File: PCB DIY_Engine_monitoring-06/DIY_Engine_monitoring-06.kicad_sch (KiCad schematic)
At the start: 62 parts, among them J1 test, J2 5V_P/S, J3 Barrel_Jack, U1 EL817, U2 EL817, U3 EL817, U4 EL817, U5 MEGA2560-Pro

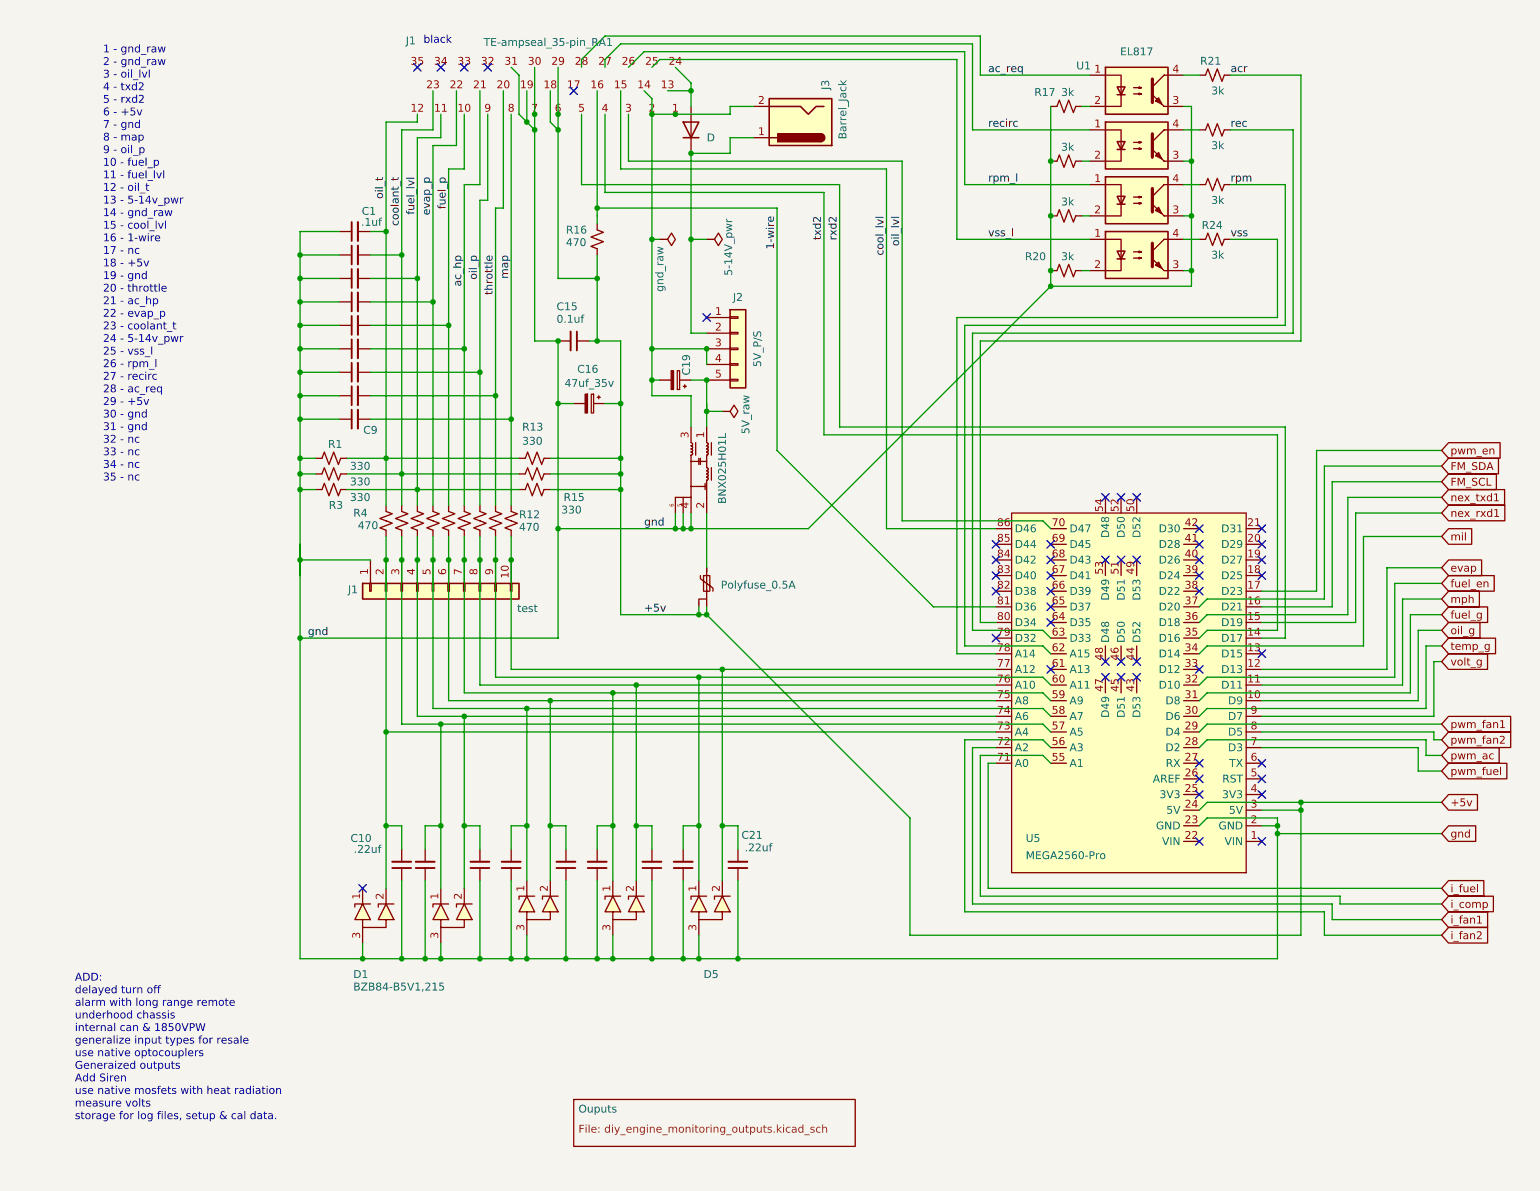
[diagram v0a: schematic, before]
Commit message: Updates include photos, harness drawings and code
Early prototype partally working.  Photos of Earlier version undergoing testing.  PCB files are for next version.
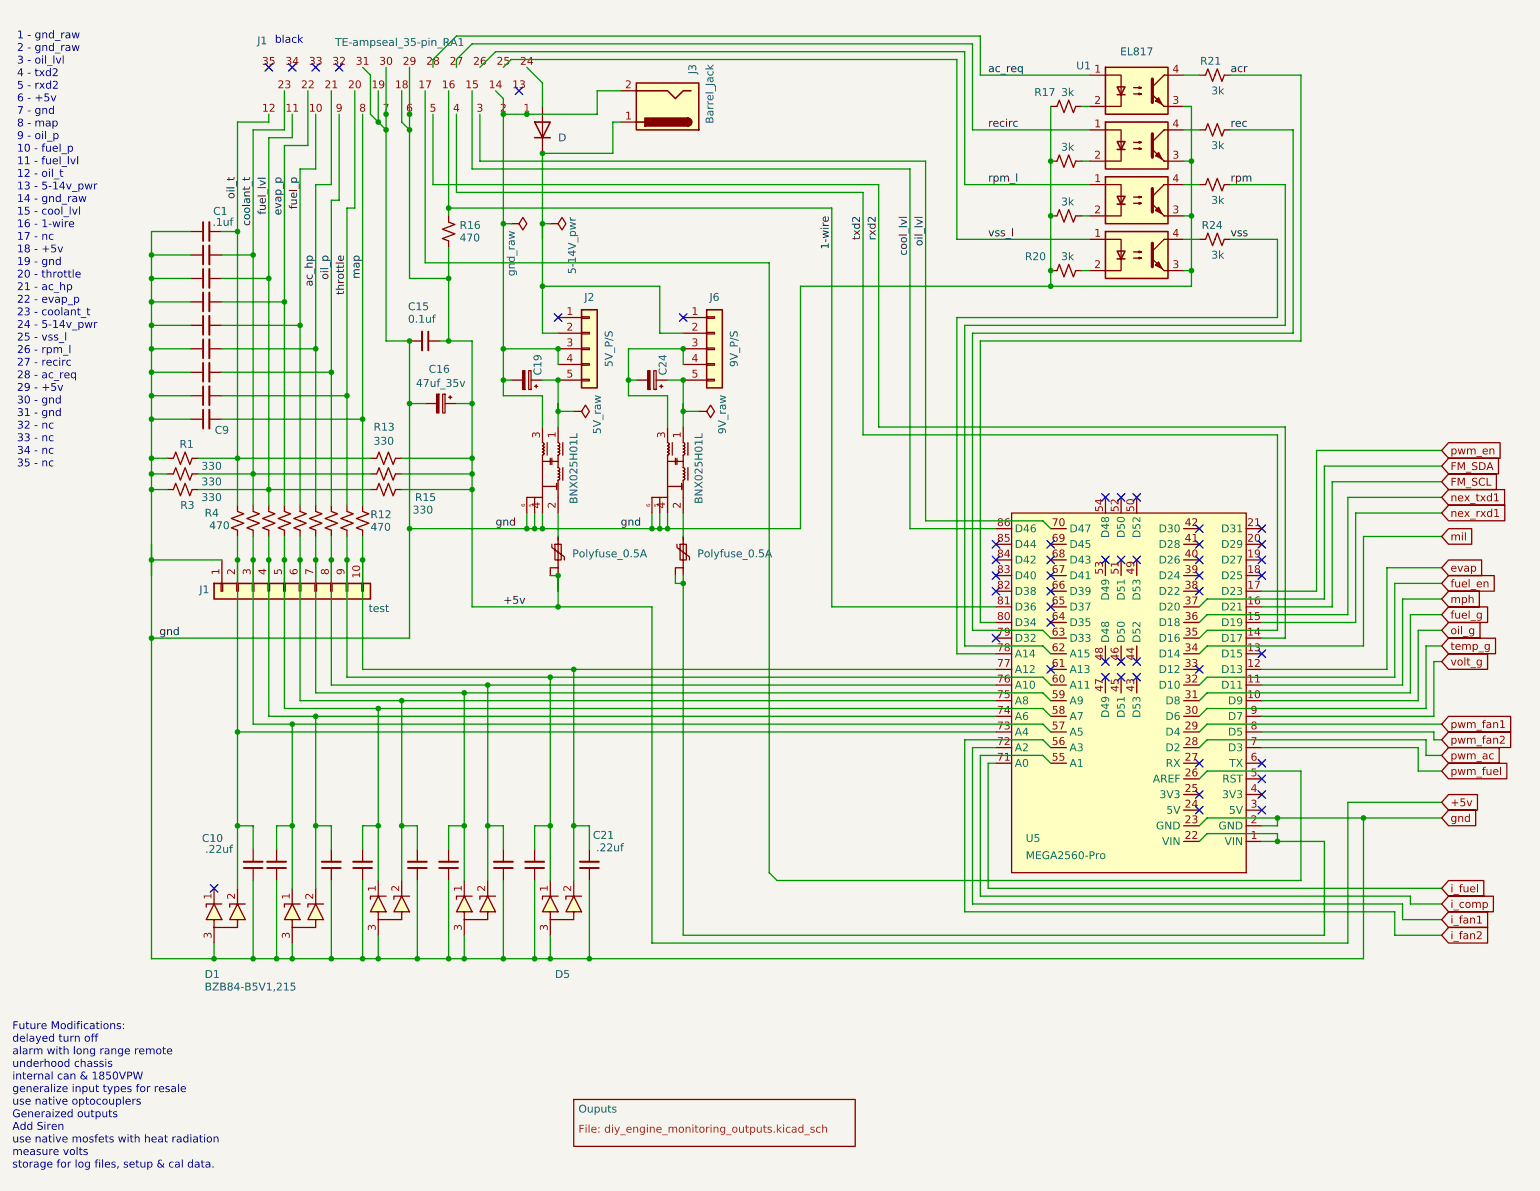
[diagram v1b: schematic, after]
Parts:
- added C24: 47uf_50v, Capacitor_THT:CP_Radial_D8.0mm_P5.00mm, symbol Device:C_Polarized_Small
- added F2: Polyfuse_0.5A, Diode_SMD:Littelfuse_PolyZen-LS, symbol ~2023:Polyfuse_Small_3pin
- added FL2: BNX025H01L, Filter:Filter_Murata_BNX025_ThermalVias, symbol ~2023:Filter_BNX025H01L
- added J6: 9V_P/S, Connector_PinSocket_2.54mm:PinSocket_1x05_P2.54mm_Vertical, symbol Connector_Generic:Conn_01x05
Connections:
- net +5v: no longer U5.24 (5V), U5.3 (5V)
- net gnd: now also FL2.4, FL2.5, FL2.6
- net at U5.1 (VIN): now also U5.22 (VIN), F2.2, F2.3
- net at U5.26 (AREF): now also TE-ampseal_35-pin_RA1.17
- net at D22.2 (A), TE-ampseal_35-pin_RA1.24: no longer TE-ampseal_35-pin_RA1.13
- net at D22.1 (K), J2.2 (Pin_2), J3.1: now also J6.2 (Pin_2)
- new net: C24.1, FL2.1, J6.5 (Pin_5)
- new net: C24.2, FL2.3, J6.3 (Pin_3), J6.4 (Pin_4)
- new net: F2.1, FL2.2
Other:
- note added: "Future Modifications: delayed turn off alarm with long range remote underhood chassis internal can & 1850VPW generalize input types for resale use native optocouplers Generaized outputs Add Siren use native mosfets with heat radiation measure volts storage for log files, setup & cal data."
- note removed: "ADD: delayed turn off alarm with long range remote underhood chassis internal can & 1850VPW generalize input types for resale use native optocouplers Generaized outputs Add Siren use native mosfets with heat radiation measure volts storage for log files, setup & cal data."
- moved on the sheet: C1, C10, C15, C16, C19, C21, C9, D1, D5, J1, J2, J3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

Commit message: Many calibrations made
Still early days of getting code fixes and analog inputs calibrated
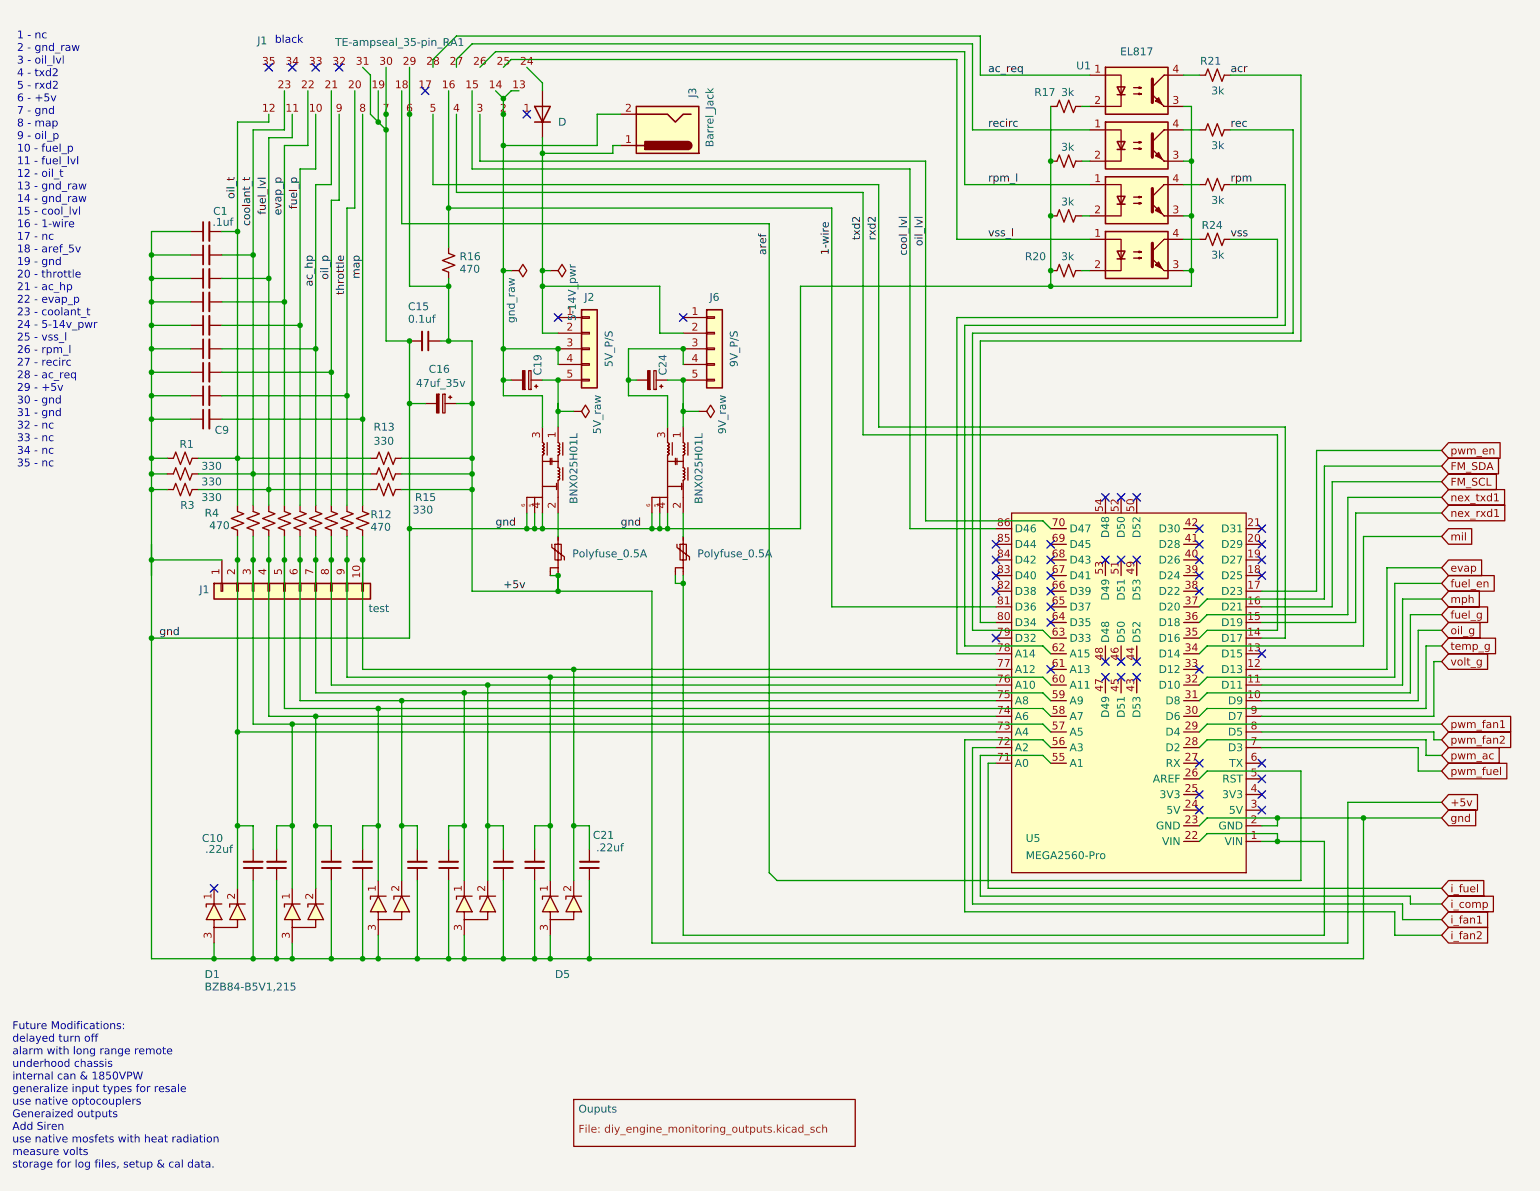
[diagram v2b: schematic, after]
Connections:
- net +5v: no longer TE-ampseal_35-pin_RA1.18
- net at TE-ampseal_35-pin_RA1.17: no longer U5.26 (AREF)
- net at C19.2, FL1.3, J2.3 (Pin_3)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: now also TE-ampseal_35-pin_RA1.13; no longer TE-ampseal_35-pin_RA1.1
- new net aref: TE-ampseal_35-pin_RA1.18, U5.26 (AREF)
- no-connect marks 50 -> 51
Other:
- note added: "1 - nc 2 - gnd_raw 3 - oil_lvl 4 - txd2 5 - rxd2 6 - +5v 7 - gnd 8 - map 9 - oil_p 10 - fuel_p 11 - fuel_lvl 12 - oil_t 13 - gnd_raw 14 - gnd_raw 15 - cool_lvl 16 - 1-wire 17 - nc 18 - aref_5v 19 - gnd 20 - throttle 21 - ac_hp 22 - evap_p 23 - coolant_t 24 - 5-14v_pwr 25 - vss_l 26 - rpm_l 27 - recirc 28 - ac_req 29 - +5v 30 - gnd 31 - gnd 32 - nc 33 - nc 34 - nc 35 - nc"
- note removed: "1 - gnd_raw 2 - gnd_raw 3 - oil_lvl 4 - txd2 5 - rxd2 6 - +5v 7 - gnd 8 - map 9 - oil_p 10 - fuel_p 11 - fuel_lvl 12 - oil_t 13 - 5-14v_pwr 14 - gnd_raw 15 - cool_lvl 16 - 1-wire 17 - nc 18 - +5v 19 - gnd 20 - throttle 21 - ac_hp 22 - evap_p 23 - coolant_t 24 - 5-14v_pwr 25 - vss_l 26 - rpm_l 27 - recirc 28 - ac_req 29 - +5v 30 - gnd 31 - gnd 32 - nc 33 - nc 34 - nc 35 - nc"
- moved on the sheet: J3, R16

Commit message: Initial testing in driven vehicle
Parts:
- added R47, R48: 3k, Resistor_SMD:R_0805_2012Metric, symbol Device:R_Small_US
- added U13: EL817, Package_DIP:DIP-4_W7.62mm, symbol Isolator:EL817
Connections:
- net gnd: now also R47.1, U13.3
- net mil: now also U5.69 (D45), R48.2
- net at C19.2, FL1.3, J2.3 (Pin_3)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: now also C24.2, FL2.3, J6.3 (Pin_3), J6.4 (Pin_4)
- net mil_l: now reaches TE-ampseal_35-pin_RA1.32
- net mil_l: now also U13.1
- new net: R47.2, U13.2
- new net: R48.1, U13.4
- no-connect marks 51 -> 50
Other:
- note added: "Future Modifications: Add MIL input delayed turn off alarm with long range remote underhood chassis internal can & 1850VPW generalize input types for resale use native optocouplers Generaized outputs Add Siren use native mosfets with heat radiation measure volts storage for log files, setup & cal data."
- note removed: "Future Modifications: delayed turn off alarm with long range remote underhood chassis internal can & 1850VPW generalize input types for resale use native optocouplers Generaized outputs Add Siren use native mosfets with heat radiation measure volts storage for log files, setup & cal data."
- moved on the sheet: C1, C10, C15, C16, C19, C21, C24, C9, D1, D5, J1, J2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
